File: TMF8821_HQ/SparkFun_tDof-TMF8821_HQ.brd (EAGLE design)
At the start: 25.4 x 12.7 mm, 48 parts, among them J4 QWIIC_RIGHT_ANGLE, J5 QWIIC_RIGHT_ANGLE

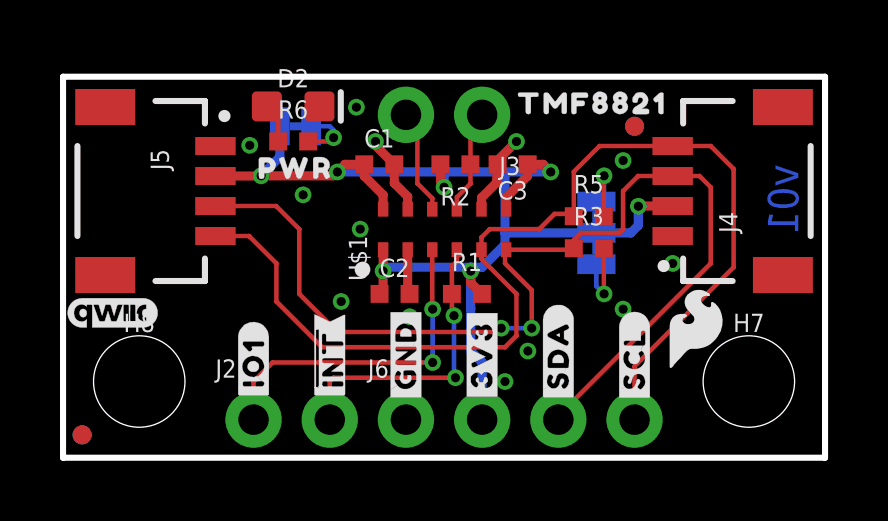
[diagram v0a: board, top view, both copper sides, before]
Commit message: Adds logos to schematic
* Moves measures to board (weren't moved when the design was put at the origin)
* Replaces IO1 silk with IO0 on GPIO0 PTH header
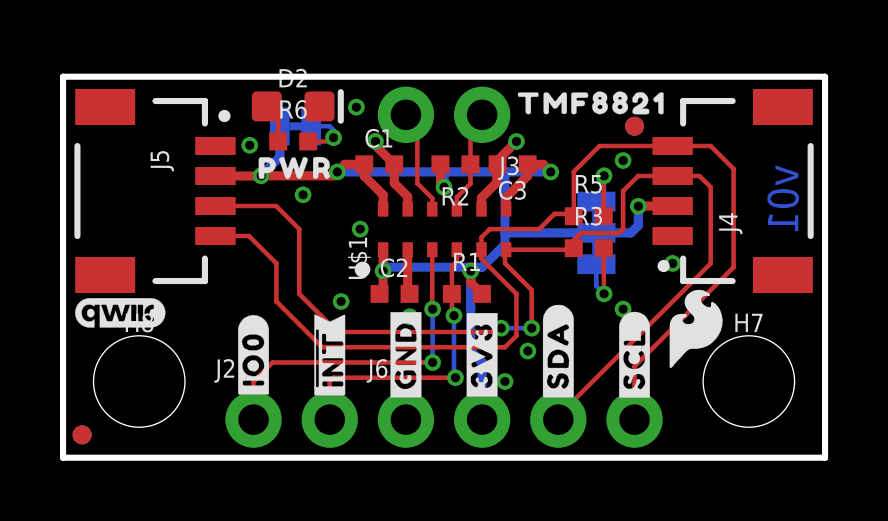
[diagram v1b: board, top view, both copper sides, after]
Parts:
- removed U$36: (no value), SparkFun-Aesthetics:QWIIC_3MM
- added LOGO1: SFE_LOGO_NAME_FLAMEBLANK, SparkFun-Aesthetics:BLANK
- added LOGO2: QWIIC_LOGO_3MM, SparkFun-Aesthetics:QWIIC_3MM
- added LOGO3: OSHW-LOGONO_SILK, SparkFun-Aesthetics:DUMMY
- U$2: device TMFHQBotSilk:#IO1#8 -> TMFHQTopSilk:#IO0#8
- moved U$2 0.13 mm to (6.35, 3.30)
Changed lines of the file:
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@@
 <layer number="115" name="ReferenceISLANDS" color="7" fill="1" visible="no" active="no"/>
 <layer number="116" name="Patch_BOT" color="9" fill="4" visible="no" active="no"/>
-<layer number="117" name="PM_Ref" color="26" fill="1" visible="yes" active="yes"/>
+<layer number="117" name="PM_Ref" color="26" fill="1" visible="no" active="yes"/>
 <layer number="118" name="Rect_Pads" color="7" fill="1" visible="no" active="no"/>
-<layer number="119" name="PF_Ref" color="31" fill="1" visible="yes" active="yes"/>
-<layer number="120" name="WFL_Ref" color="25" fill="1" visible="yes" active="yes"/>
+<layer number="119" name="PF_Ref" color="31" fill="1" visible="no" active="yes"/>
+<layer number="120" name="WFL_Ref" color="25" fill="1" visible="no" active="yes"/>
 <layer number="121" name="_tsilk" color="7" fill="1" visible="no" active="no"/>
 <layer number="122" name="_bsilk" color="7" fill="1" visible="no" active="no"/>
@@
 <wire x1="25.4" y1="0" x2="0" y2="0" width="0.2032" layer="20"/>
 <text x="24.511" y="9.779" size="1.016" layer="16" font="vector" ratio="20" rot="SMR270">v01</text>
-<text x="37.084" y="21.082" size="1.778" layer="47" font="vector">Units in Inches</text>
+<text x="4.064" y="-5.588" size="1.778" layer="47" font="vector">Units in Inches</text>
 <text x="15.367" y="-13.081" size="1.778" layer="51" font="vector">Elias Santistevan</text>
-<dimension x1="33.02" y1="39.37" x2="58.42" y2="39.37" x3="45.72" y3="45.72" textsize="1.778" layer="47" unit="inch"/>
-<dimension x1="33.02" y1="26.67" x2="33.02" y2="39.37" x3="24.13" y3="33.02" textsize="1.778" layer="47" unit="inch"/>
-<dimension x1="38.1" y1="35.56" x2="38.1" y2="26.67" x3="27.94" y3="31.115" textsize="1.778" layer="47" unit="inch"/>
-<dimension x1="45.72" y1="34.29" x2="45.72" y2="26.67" x3="31.75" y3="30.48" textsize="1.778" layer="47" unit="inch"/>
-<dimension x1="55.88" y1="29.21" x2="55.88" y2="26.67" x3="66.04" y3="27.94" textsize="1.778" layer="47" unit="inch"/>
-<dimension x1="55.88" y1="29.21" x2="58.42" y2="29.21" x3="57.15" y3="41.91" textsize="1.778" layer="47" unit="inch"/>
-<dimension x1="45.72" y1="34.29" x2="33.02" y2="34.29" x3="39.37" y3="41.91" textsize="1.778" layer="47" unit="inch"/>
+<dimension x1="0" y1="12.7" x2="25.4" y2="12.7" x3="12.7" y3="19.05" textsize="1.778" layer="47" unit="inch"/>
+<dimension x1="0" y1="0" x2="0" y2="12.7" x3="-8.89" y3="6.35" textsize="1.778" layer="47" unit="inch"/>
+<dimension x1="5.08" y1="8.89" x2="5.08" y2="0" x3="-5.08" y3="4.445" textsize="1.778" layer="47" unit="inch"/>
+<dimension x1="12.7" y1="7.62" x2="12.7" y2="0" x3="-1.27" y3="3.81" textsize="1.778" layer="47" unit="inch"/>
+<dimension x1="22.86" y1="2.54" x2="22.86" y2="0" x3="33.02" y3="1.27" textsize="1.778" layer="47" unit="inch"/>
+<dimension x1="22.86" y1="2.54" x2="25.4" y2="2.54" x3="24.13" y3="15.24" textsize="1.778" layer="47" unit="inch"/>
+<dimension x1="12.7" y1="7.62" x2="0" y2="7.62" x3="6.35" y3="15.24" textsize="1.778" layer="47" unit="inch"/>
 </plain>
 <attributes>
@@
 <element name="U$34" library="SparkFun-Aesthetics" package="OSHW-LOGO-MINI" value="" x="23.749" y="10.922" smashed="yes" rot="MR0"/>
 <element name="U$35" library="SparkFun-Aesthetics" package="SFE_LOGO_FLAME_.1" value="" x="21.082" y="4.318" smashed="yes"/>
-<element name="U$36" library="SparkFun-Aesthetics" package="QWIIC_3MM" value="" x="1.651" y="4.826" smashed="yes"/>
 <element name="U$37" library="TMFHQTopSilk" package="#3V3#0" value="" x="13.97" y="3.429" smashed="yes" rot="R90"/>
 <element name="U$38" library="TMFHQTopSilk" package="#GND#4" value="" x="11.43" y="3.429" smashed="yes" rot="R90"/>
@@
 <element name="U$40" library="TMFHQTopSilk" package="#SDA#6" value="" x="16.51" y="3.429" smashed="yes" rot="R90"/>
 <element name="U$43" library="TMFHQTopSilk" package="PWR8821882023" value="" x="7.747" y="9.652" smashed="yes"/>
-<element name="U$2" library="TMFHQBotSilk" package="#IO1#8" value="" x="6.35" y="3.175" smashed="yes" rot="R90"/>
 <element name="U$3" library="TMFHQBotSilk" package="##INT##9" value="" x="8.89" y="3.302" smashed="yes" rot="R90"/>
 <element name="U$4" library="TMFHQTopSilk" package="##INT##8" value="" x="8.89" y="3.302" smashed="yes" rot="MR270"/>
@@
 <element name="U$8" library="TMFHQTopSilk" package="TMF882188210" value="" x="5.207" y="6.858" smashed="yes" rot="MR0"/>
 <element name="U$9" library="TMFHQBotSilk" package="TMF882113" value="" x="17.653" y="11.811" smashed="yes"/>
+<element name="LOGO1" library="SparkFun-Aesthetics" package="BLANK" value="SFE_LOGO_NAME_FLAMEBLANK" x="-11.938" y="-12.954" smashed="yes"/>
+<element name="LOGO2" library="SparkFun-Aesthetics" package="QWIIC_3MM" value="QWIIC_LOGO_3MM" x="1.905" y="4.826" smashed="yes"/>
+<element name="LOGO3" library="SparkFun-Aesthetics" package="DUMMY" value="OSHW-LOGONO_SILK" x="-11.938" y="-12.954" smashed="yes"/>
+<element name="U$2" library="TMFHQTopSilk" package="#IO0#8" value="" x="6.35" y="3.302" smashed="yes" rot="R90"/>
 </elements>
 <signals>
